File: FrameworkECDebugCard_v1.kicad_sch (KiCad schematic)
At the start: 18 parts, among them P1 USB_C_Plug_USB2.0, P2 USB_B_Micro, U1 FT230XS

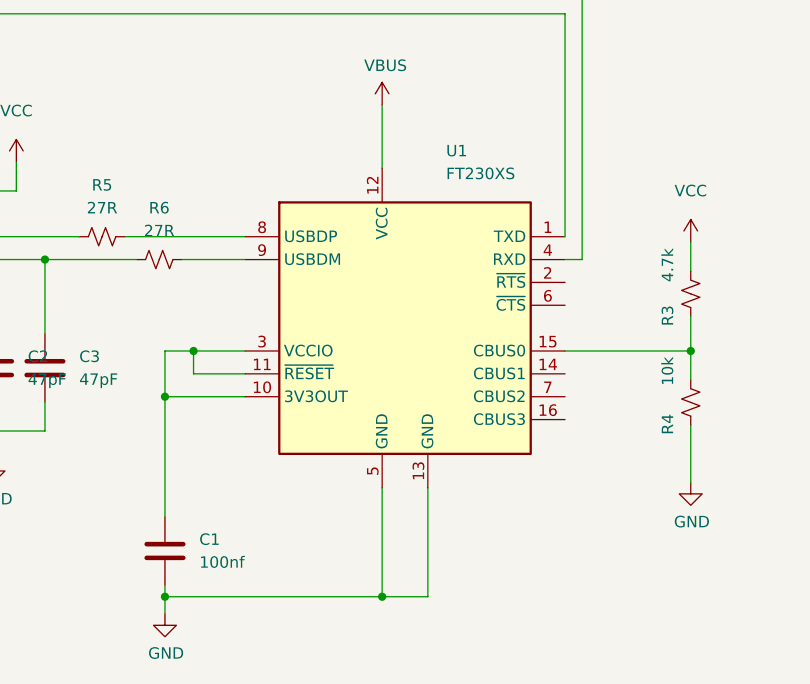
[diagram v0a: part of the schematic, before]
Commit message: v1.1: switch to FT230XQ (QFN) and 0402 components instead of 0603
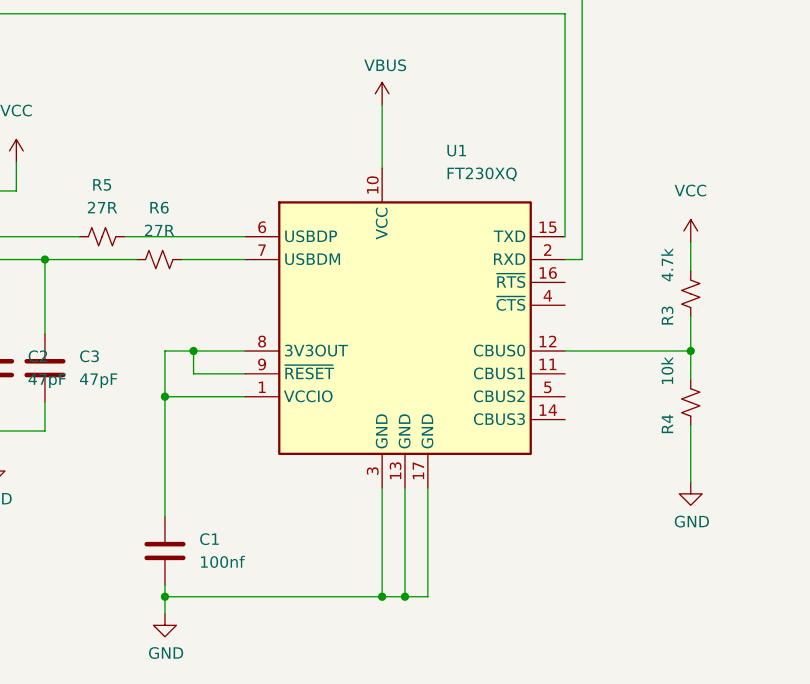
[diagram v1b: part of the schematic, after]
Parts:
- C1, C2, C3: footprint Capacitor_SMD:C_0603_1608Metric -> Capacitor_SMD:C_0402_1005Metric
- R1, R2, R3, R4, R5, R6: footprint Resistor_SMD:R_0603_1608Metric -> Resistor_SMD:R_0402_1005Metric
- U1: value FT230XS -> FT230XQ; footprint Package_SO:SSOP-16_3.9x4.9mm_P0.635mm -> Package_DFN_QFN:QFN-16-1EP_4x4mm_P0.65mm_EP2.1x2.1mm; symbol Interface_USB:FT230XS -> Interface_USB:FT230XQ
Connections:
- net GND: now also U1.17 (GND), U1.3 (GND); no longer U1.5 (GND)
- net VBUS: now also U1.10 (VCC); no longer U1.12 (VCC)
- net at P1.A8 (DOUT): now also U1.2 (RXD); no longer U1.4 (RXD)
- net at P1.B8 (DIN): now also U1.15 (TXD); no longer U1.1 (TXD)
- net at R5.2: now also U1.6 (USBDP); no longer U1.8 (USBDP)
- net at R3.1, R4.2: now also U1.12 (CBUS0); no longer U1.15 (CBUS0)
- net at R6.2: now also U1.7 (USBDM); no longer U1.9 (USBDM)
- new net: C1.1, U1.1 (VCCIO), U1.8 (3V3OUT), U1.9 (~{RESET})
- now unconnected: U1.11 (~{RESET})
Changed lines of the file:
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@@
   (junction (at 111.125 50.165) (diameter 0) (color 0 0 0 0)
   )
+  (junction (at 156.845 90.17) (diameter 0) (color 0 0 0 0)
+  )
   (junction (at 41.91 78.74) (diameter 0) (color 0 0 0 0)
   )
@@
     (stroke (width 0) (type default) (color 0 0 0 0))
   )
-  (wire (pts (xy 159.385 90.17) (xy 154.305 90.17))
+  (wire (pts (xy 159.385 90.17) (xy 156.845 90.17))
     (stroke (width 0) (type default) (color 0 0 0 0))
   )
@@
     (stroke (width 0) (type default) (color 0 0 0 0))
   )
+  (wire (pts (xy 156.845 90.17) (xy 154.305 90.17))
+    (stroke (width 0) (type default) (color 0 0 0 0))
+  )
   (wire (pts (xy 159.385 78.105) (xy 159.385 90.17))
     (stroke (width 0) (type default) (color 0 0 0 0))
@@
   )
   (wire (pts (xy 72.39 45.72) (xy 73.66 45.72))
+    (stroke (width 0) (type default) (color 0 0 0 0))
+  )
+  (wire (pts (xy 156.845 78.105) (xy 156.845 90.17))
     (stroke (width 0) (type default) (color 0 0 0 0))
   )
@@
       (effects (font (size 1.27 1.27)) (justify left))
     )
-    (property "Footprint" "Resistor_SMD:R_0603_1608Metric" (id 2) (at 68.58 43.18 0)
+    (property "Footprint" "Resistor_SMD:R_0402_1005Metric" (id 2) (at 68.58 43.18 0)
       (effects (font (size 1.27 1.27)) hide)
     )
@@
       (effects (font (size 1.27 1.27)) (justify left))
     )
-    (property "Footprint" "Capacitor_SMD:C_0603_1608Metric" (id 2) (at 112.0902 68.58 0)
+    (property "Footprint" "Capacitor_SMD:C_0402_1005Metric" (id 2) (at 112.0902 68.58 0)
       (effects (font (size 1.27 1.27)) hide)
     )
@@
     (property "Reference" "R5" (id 0) (at 123.19 44.45 90))
     (property "Value" "27R" (id 1) (at 123.19 46.99 90))
-    (property "Footprint" "Resistor_SMD:R_0603_1608Metric" (id 2) (at 123.19 50.165 0)
+    (property "Footprint" "Resistor_SMD:R_0402_1005Metric" (id 2) (at 123.19 50.165 0)
       (effects (font (size 1.27 1.27)) hide)
     )
@@
       (effects (font (size 1.27 1.27)) (justify left))
     )
-    (property "Footprint" "Resistor_SMD:R_0603_1608Metric" (id 2) (at 69.85 45.72 0)
+    (property "Footprint" "Resistor_SMD:R_0402_1005Metric" (id 2) (at 69.85 45.72 0)
       (effects (font (size 1.27 1.27)) hide)
     )
@@
       (effects (font (size 1.27 1.27)) (justify left))
     )
-    (property "Footprint" "Capacitor_SMD:C_0603_1608Metric" (id 2) (at 117.8052 68.58 0)
+    (property "Footprint" "Capacitor_SMD:C_0402_1005Metric" (id 2) (at 117.8052 68.58 0)
       (effects (font (size 1.27 1.27)) hide)
     )
@@
       (effects (font (size 1.27 1.27)) (justify left))
     )
-    (property "Footprint" "Resistor_SMD:R_0603_1608Metric" (id 2) (at 188.595 56.515 0)
+    (property "Footprint" "Resistor_SMD:R_0402_1005Metric" (id 2) (at 188.595 56.515 0)
       (effects (font (size 1.27 1.27)) hide)
     )
@@
     (property "Reference" "R6" (id 0) (at 129.54 46.99 90))
     (property "Value" "27R" (id 1) (at 129.54 49.53 90))
-    (property "Footprint" "Resistor_SMD:R_0603_1608Metric" (id 2) (at 129.54 52.705 0)
+    (property "Footprint" "Resistor_SMD:R_0402_1005Metric" (id 2) (at 129.54 52.705 0)
       (effects (font (size 1.27 1.27)) hide)
     )
@@
       (effects (font (size 1.27 1.27)) (justify left))
     )
-    (property "Footprint" "Resistor_SMD:R_0603_1608Metric" (id 2) (at 188.595 68.58 0)
+    (property "Footprint" "Resistor_SMD:R_0402_1005Metric" (id 2) (at 188.595 68.58 0)
       (effects (font (size 1.27 1.27)) hide)
     )
@@
     (pin "1")
   )
-  (symbol (lib_id "Interface_USB:FT230XS") (at 156.845 60.325 0) (unit 1)
+  (symbol (lib_id "Interface_USB:FT230XQ") (at 156.845 60.325 0) (unit 1)
     (in_bom yes) (on_board yes) (fields_autoplaced)
     (property "Reference" "U1" (id 0) (at 161.4044 40.64 0)
       (effects (font (size 1.27 1.27)) (justify left))
     )
-    (property "Value" "FT230XS" (id 1) (at 161.4044 43.18 0)
-      (effects (font (size 1.27 1.27)) (justify left))
-    )
-    (property "Footprint" "Package_SO:SSOP-16_3.9x4.9mm_P0.635mm" (id 2) (at 182.245 75.565 0)
+    (property "Value" "FT230XQ" (id 1) (at 161.4044 43.18 0)
+      (effects (font (size 1.27 1.27)) (justify left))
+    )
+    (property "Footprint" "Package_DFN_QFN:QFN-16-1EP_4x4mm_P0.65mm_EP2.1x2.1mm" (id 2) (at 191.135 75.565 0)
       (effects (font (size 1.27 1.27)) hide)
     )
@@
     (pin "15")
     (pin "16")
+    (pin "17")
     (pin "2")
     (pin "3")
@@
       (effects (font (size 1.27 1.27)) (justify left))
     )
-    (property "Footprint" "Capacitor_SMD:C_0603_1608Metric" (id 2) (at 131.1402 88.9 0)
+    (property "Footprint" "Capacitor_SMD:C_0402_1005Metric" (id 2) (at 131.1402 88.9 0)
       (effects (font (size 1.27 1.27)) hide)
     )
@@
     )
     (path "/e4410938-748d-4f87-a5a0-2f41e55e999c"
-      (reference "C1") (unit 1) (value "100nf") (footprint "Capacitor_SMD:C_0603_1608Metric")
+      (reference "C1") (unit 1) (value "100nf") (footprint "Capacitor_SMD:C_0402_1005Metric")
     )
     (path "/3406007f-362d-417a-ba62-f33ae8f5a03a"
-      (reference "C2") (unit 1) (value "47pF") (footprint "Capacitor_SMD:C_0603_1608Metric")
+      (reference "C2") (unit 1) (value "47pF") (footprint "Capacitor_SMD:C_0402_1005Metric")
     )
     (path "/685f0971-12c4-4d07-8eec-3ff16ff9a7d3"
-      (reference "C3") (unit 1) (value "47pF") (footprint "Capacitor_SMD:C_0603_1608Metric")
+      (reference "C3") (unit 1) (value "47pF") (footprint "Capacitor_SMD:C_0402_1005Metric")
     )
     (path "/00000000-0000-0000-0000-00005fdb1a76"
@@
     )
     (path "/00000000-0000-0000-0000-00005fd77c84"
-      (reference "R1") (unit 1) (value "5.1k") (footprint "Resistor_SMD:R_0603_1608Metric")
+      (reference "R1") (unit 1) (value "5.1k") (footprint "Resistor_SMD:R_0402_1005Metric")
     )
     (path "/55f95895-f458-441d-b110-8ef9d0678a01"
-      (reference "R2") (unit 1) (value "5.1k") (footprint "Resistor_SMD:R_0603_1608Metric")
+      (reference "R2") (unit 1) (value "5.1k") (footprint "Resistor_SMD:R_0402_1005Metric")
     )
     (path "/6d411771-d4d2-4689-be79-f0360a18a1f2"
-      (reference "R3") (unit 1) (value "4.7k") (footprint "Resistor_SMD:R_0603_1608Metric")
+      (reference "R3") (unit 1) (value "4.7k") (footprint "Resistor_SMD:R_0402_1005Metric")
     )
     (path "/7c4c4aa8-29f6-4b39-a2c5-1814b134be66"
-      (reference "R4") (unit 1) (value "10k") (footprint "Resistor_SMD:R_0603_1608Metric")
+      (reference "R4") (unit 1) (value "10k") (footprint "Resistor_SMD:R_0402_1005Metric")
     )
     (path "/555c44f4-64ed-4c28-9279-22a03f27c9dd"
-      (reference "R5") (unit 1) (value "27R") (footprint "Resistor_SMD:R_0603_1608Metric")
+      (reference "R5") (unit 1) (value "27R") (footprint "Resistor_SMD:R_0402_1005Metric")
     )
     (path "/79632d0a-2b4d-433b-b855-fd528772c1aa"
-      (reference "R6") (unit 1) (value "27R") (footprint "Resistor_SMD:R_0603_1608Metric")
+      (reference "R6") (unit 1) (value "27R") (footprint "Resistor_SMD:R_0402_1005Metric")
     )
     (path "/00000000-0000-0000-0000-0000606a89a3"
@@
     )
     (path "/e0d801af-4ad0-4d87-acdb-c981e463453f"
-      (reference "U1") (unit 1) (value "FT230XS") (footprint "Package_SO:SSOP-16_3.9x4.9mm_P0.635mm")
-    )
-  )
+      (reference "U1") (unit 1) (value "FT230XQ") (footprint "Package_DFN_QFN:QFN-16-1EP_4x4mm_P0.65mm_EP2.1x2.1mm")
+    )
+  )

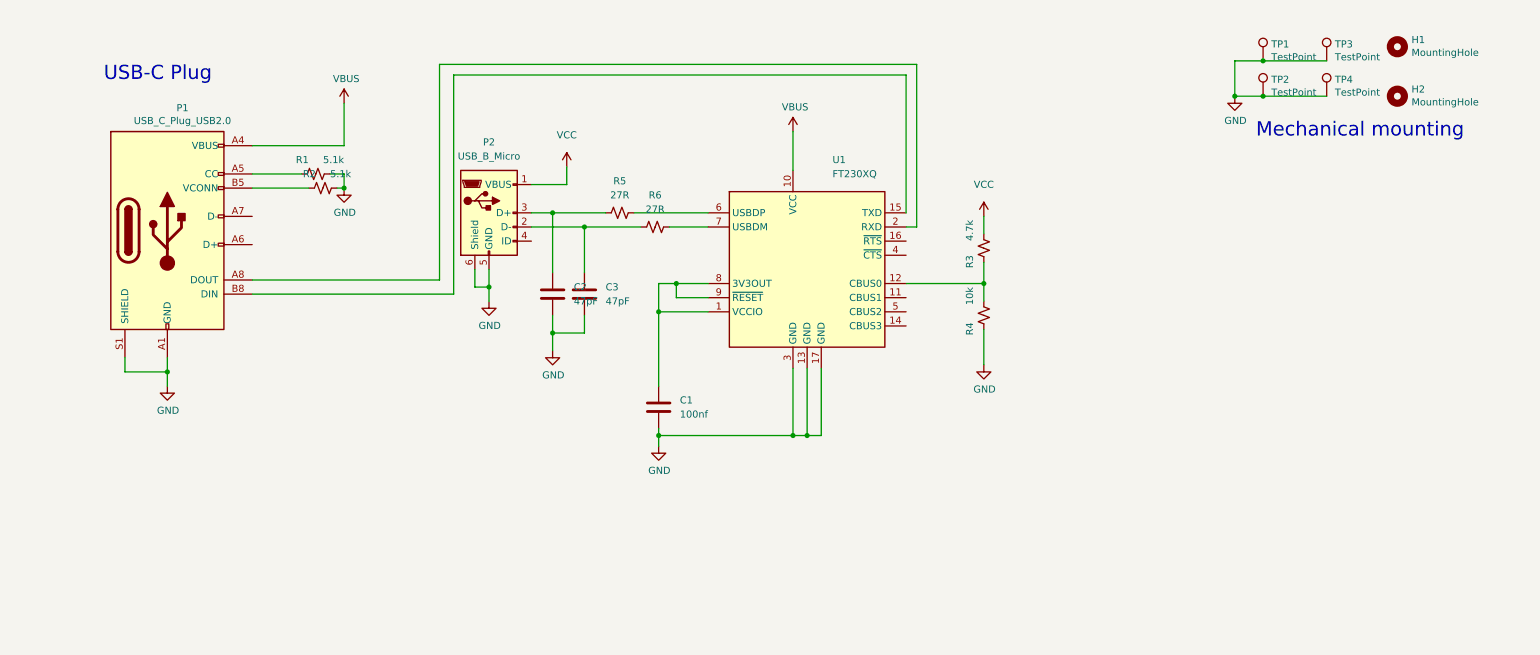
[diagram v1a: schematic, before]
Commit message: Schematic: clarify VBUS_{HOST,DEV}, reorganize to avoid flyover wires
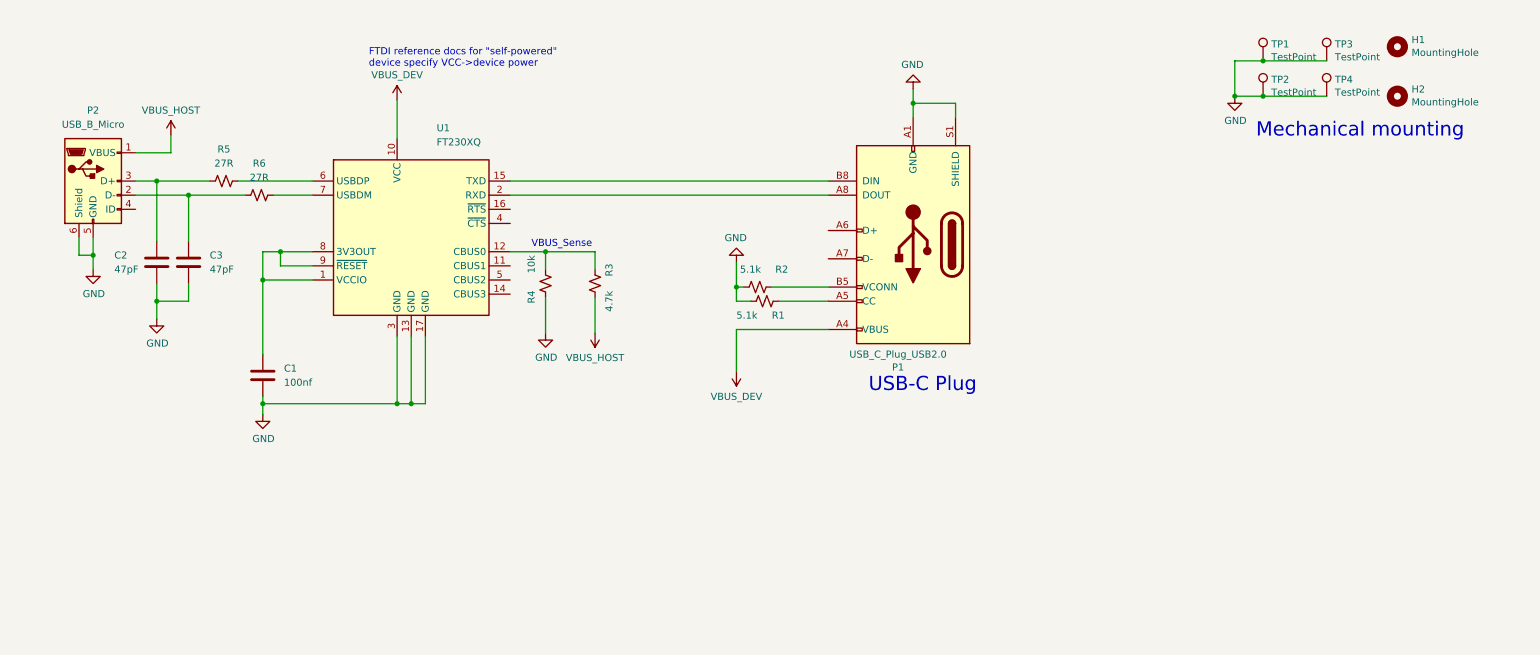
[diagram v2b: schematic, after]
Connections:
- net VBUS renamed VBUS_DEV
- net VCC renamed VBUS_HOST
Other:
- note added: "FTDI reference docs for "self-powered" device specify VCC->device power"
- note added: "VBUS_Sense"
- title: EC CCD Debug Card -> EC Debug Card
- moved on the sheet: C1, C2, C3, P1, P2, R1, R2, R3, R4, R5, R6, U1

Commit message: Rework board per Kieran's suggestions
- Route the USB differential pairs together, and without vias
	- Had to move back to the SSOP package because the QFN package
	  would require a crossover (yes, no, it doesn't make any sense)
- Ground fill
- Hand-route
- Redistribute passives to be more reasonably laid out
- Power the FTDI chip off VBUS_HOST instead of VBUS_DEV
- Add TX/RX LEDs
- Add a ferrite bead
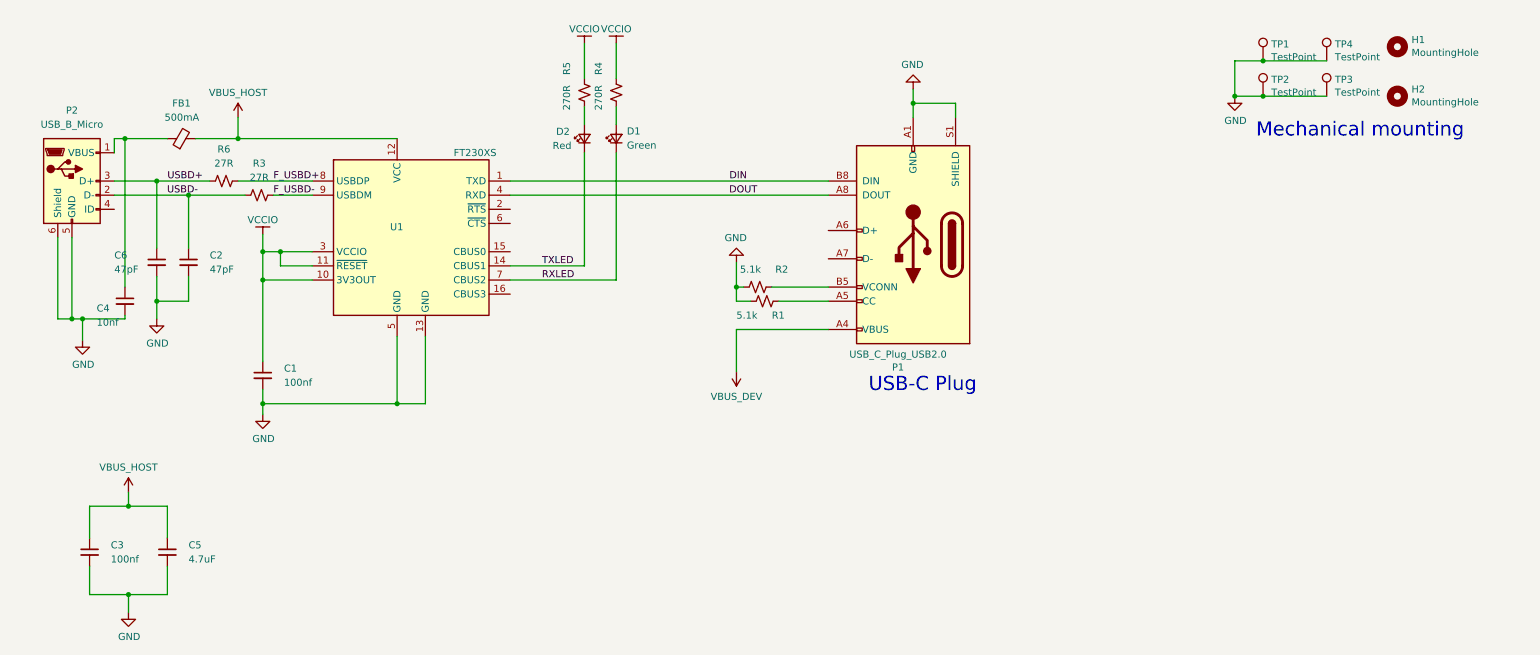
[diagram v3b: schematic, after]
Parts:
- removed R3: 4.7k, Resistor_SMD:R_0402_1005Metric, symbol Device:R_Small_US
- added C3: 100nf, Capacitor_SMD:C_0402_1005Metric, symbol Device:C_Small
- added C4: 10nf, Capacitor_SMD:C_0402_1005Metric, symbol Device:C_Small
- added C5: 4.7uF, Capacitor_SMD:C_0402_1005Metric, symbol Device:C_Small
- added D1: Green, LED_SMD:LED_0603_1608Metric, symbol Device:LED_Small
- added D2: Red, LED_SMD:LED_0603_1608Metric, symbol Device:LED_Small
- added FB1: 500mA, Inductor_SMD:L_0402_1005Metric, symbol Device:FerriteBead_Small
- added R5: 270R, Resistor_SMD:R_0402_1005Metric, symbol Device:R_Small_US
- C1: symbol Device:C -> Device:C_Small
- C2: renamed from C3; symbol Device:C -> Device:C_Small
- C6: renamed from C2; symbol Device:C -> Device:C_Small
- R4: value 10k -> 270R
- U1: value FT230XQ -> FT230XS; footprint Package_DFN_QFN:QFN-16-1EP_4x4mm_P0.65mm_EP2.1x2.1mm -> Package_SO:SSOP-16_3.9x4.9mm_P0.635mm; symbol Interface_USB:FT230XQ -> Interface_USB:FT230XS
- renumbered R6 to R3, R5 to R6, TP4 to TP3, TP3 to TP4
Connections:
- net GND: now also U1.5 (GND), C3.2, C4.2, C5.2; no longer R4.1, U1.17 (GND), U1.3 (GND)
- net VBUS_DEV: no longer U1.10 (VCC)
- net VBUS_HOST: now also U1.12 (VCC), C3.1, C5.1, FB1.2; no longer P2.1 (VBUS)
- net at U1.2 (~{RTS}): no longer P1.A8 (DOUT)
- net at U1.15 (CBUS0): no longer P1.B8 (DIN)
- net USBD+: now reaches C6.1, P2.3 (D+), R6.1
- net at U1.6 (~{CTS}): no longer R6.2
- net USBD-: now reaches C2.1, P2.2 (D-), R3.1
- net at R4.2: now also D1.2 (A); no longer U1.12 (CBUS0)
- net F_USBD-: now reaches R3.2
- net F_USBD-: now also U1.9 (USBDM); no longer U1.7 (USBDM)
- net VCCIO: now reaches U1.11 (~{RESET})
- net VCCIO: now also C1.1, R4.1, U1.10 (3V3OUT), U1.3 (VCCIO), R5.1
- net TXLED: now reaches U1.14 (CBUS1)
- net TXLED: now also D2.1 (K)
- net DOUT: now reaches U1.4 (RXD)
- net DOUT: now also P1.A8 (DOUT)
- new net: D2.2 (A), R5.2
- new net: C4.1, FB1.1, P2.1 (VBUS)
- new net DIN: P1.B8 (DIN), U1.1 (TXD)
- new net F_USBD+: R6.2, U1.8 (USBDP)
- new net RXLED: D1.1 (K), U1.7 (CBUS2)
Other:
- note removed: "FTDI reference docs for "self-powered" device specify VCC->device power"
- note removed: "VBUS_Sense"
- moved on the sheet: P2
